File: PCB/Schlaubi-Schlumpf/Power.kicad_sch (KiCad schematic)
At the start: 33 parts, among them IC2 TP4056, IC3 TPS7A8801RTJR, IC7 LM2775QDSGRQ1, Q1 DMG2305

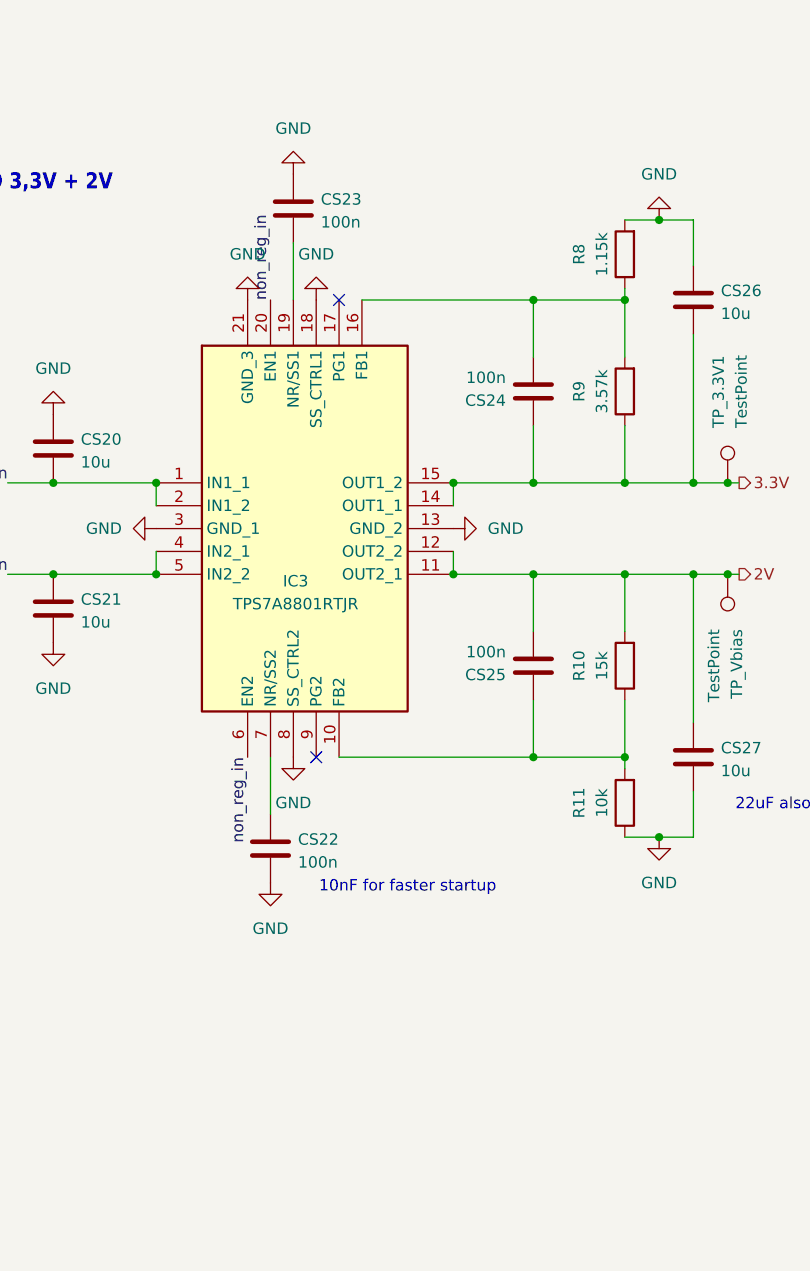
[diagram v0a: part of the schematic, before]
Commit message: added IMU
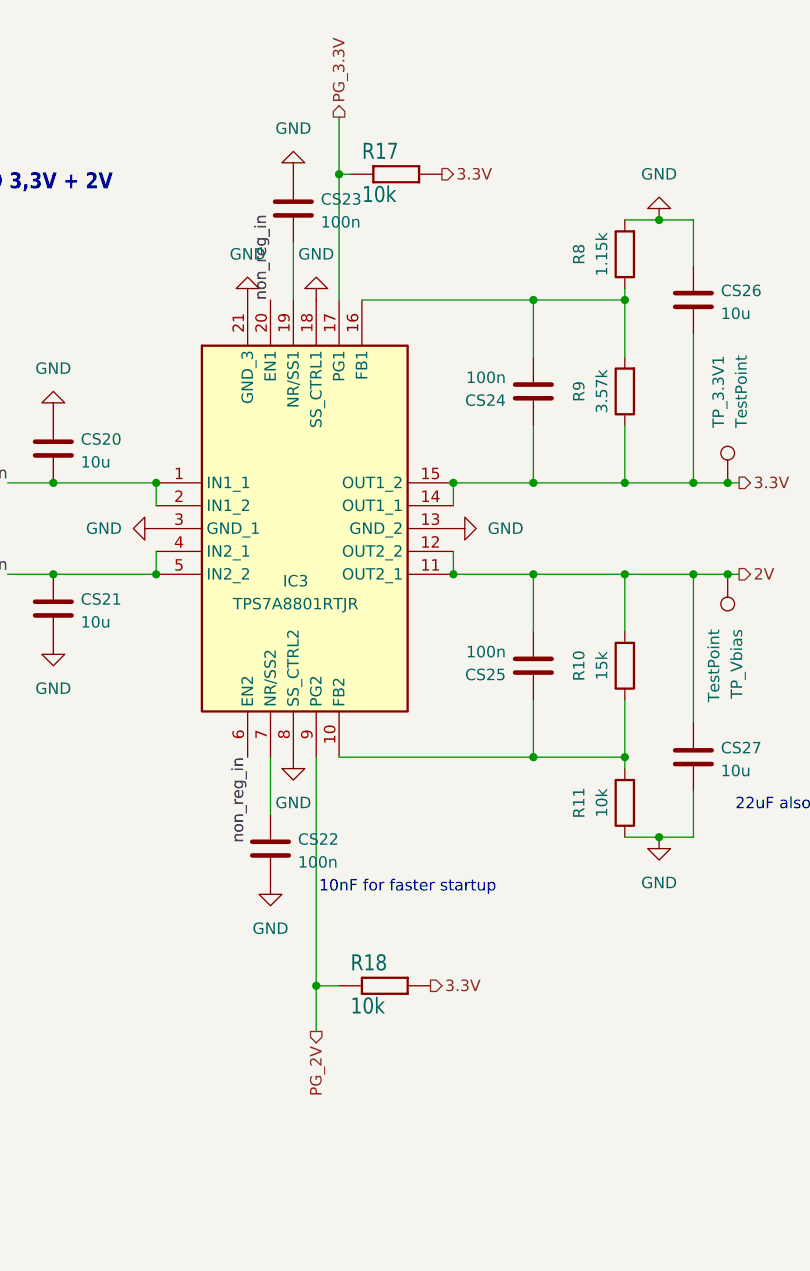
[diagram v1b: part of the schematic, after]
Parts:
- added R17, R18: 10k, Resistor_SMD:R_0603_1608Metric, symbol MiniLev-eagle-import:R-EU_R0805
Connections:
- net 3.3V: now also R17.2, R18.2
- net PG_3.3V: now reaches IC3.17 (PG1)
- net PG_3.3V: now also R17.1
- net PG_2V: now reaches IC3.9 (PG2)
- net PG_2V: now also R18.1
- no-connect marks 4 -> 2

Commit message: v1
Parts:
- removed R17, R18, R5: 10k, Resistor_SMD:R_0603_1608Metric, symbol MiniLev-eagle-import:R-EU_R0805
- added J4: Conn_01x02_Pin, Connector_JST:JST_PH_B2B-PH-K_1x02_P2.00mm_Vertical, symbol Connector:Conn_01x02_Pin
- added R17: 10k, Resistor_SMD:R_0603_1608Metric, symbol Device:R
- added TP_GND2: TestPoint, TestPoint:TestPoint_Pad_D1.0mm, symbol Connector:TestPoint
- C1: footprint Capacitor_SMD:C_0805_2012Metric -> Capacitor_SMD:C_0603_1608Metric
- CS22, CS23, CS24, CS25: value 100n -> 10n
- D2: value LED -> LED_R; footprint LED_SMD:LED_0805_2012Metric -> LED_SMD:LED_0603_1608Metric
- IC2: footprint MiniLev:SOP-8 -> TP4056:SOP127P600X175-9N
- IC3: footprint QFN50P400X400X80-21N-D -> TPS7A8801RTJR:QFN50P400X400X80-21N-D
- IC7: footprint SON50P200X200X80-9N -> LM2775QDSGRQ1:SON50P200X200X80-9N
- Q1: footprint MiniLev:SOT23-WIDE -> DMG2305UX:DMG2305UX
- TP_3.3V1: footprint TestPoint:TestPoint_THTPad_D1.0mm_Drill0.5mm -> TestPoint:TestPoint_Pad_D1.0mm
- TP_Vbias1: renamed from TP_Vbias; footprint TestPoint:TestPoint_THTPad_D1.0mm_Drill0.5mm -> TestPoint:TestPoint_Pad_D1.0mm
- renumbered C_Chargepump to CCHARGE1
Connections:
- net VBUS is gone; now on net Vbus: C8.1, D2.2 (A), IC2.4 (VCC), IC2.8 (CE)
- net Bat+: now also J4.2 (Pin_2)
- net GND: now also IC2.9 (EPAD), J4.1 (Pin_1), R17.1, TP_GND2.1
- net Vbus: now also R17.2
- net at C1.2, D1.1 (K), Q1.2 (S): now also S1.3; no longer S1.1
- net PG_2V: no longer names the net of IC3.9 (PG2)
- net PG_3.3V: no longer names the net of IC3.17 (PG1)
- no-connect marks 2 -> 4
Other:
- moved on the sheet: CS20, CS21, CS22, CS24, CS25, CS26, CS27, IC3, R10, R11, R8, R9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

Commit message: updates
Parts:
- CS22, CS23: value 10n -> 100n
- TP_3.3V1, TP_GND2, TP_Vbias1: footprint TestPoint:TestPoint_Pad_D1.0mm -> TestPoint:TestPoint_Pad_D1.5mm
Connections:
- net Bat+: now also J4.1 (Pin_1); no longer J4.2 (Pin_2)
- net GND: now also J4.2 (Pin_2); no longer J4.1 (Pin_1)
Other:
- moved on the sheet: J4, TP_GND2
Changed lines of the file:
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@@
 	(wire
 		(pts
+			(xy 105.41 93.98) (xy 105.41 99.06)
+		)
+		(stroke
+			(width 0)
+			(type default)
+		)
+	)
+	(wire
+		(pts
 			(xy 52.07 41.91) (xy 57.15 41.91)
 		)
@@
 	(wire
 		(pts
-			(xy 105.41 93.98) (xy 105.41 99.06)
-		)
-		(stroke
-			(width 0)
-			(type default)
-		)
-	)
-	(wire
-		(pts
 			(xy 44.45 99.06) (xy 46.99 99.06)
 		)
@@
 			)
 		)
-		(property "Footprint" "TestPoint:TestPoint_Pad_D1.0mm"
+		(property "Footprint" "TestPoint:TestPoint_Pad_D1.5mm"
 			(at 257.81 72.39 0)
 			(effects
@@
 	(symbol
 		(lib_id "Connector:TestPoint")
-		(at 278.13 64.77 0)
+		(at 233.68 152.4 0)
 		(unit 1)
 		(exclude_from_sim no)
@@
 		(dnp no)
 		(property "Reference" "TP_GND2"
-			(at 277.114 58.674 90)
+			(at 232.664 146.304 90)
 			(effects
 				(font
@@
 		)
 		(property "Value" "TestPoint"
-			(at 279.654 58.674 90)
+			(at 235.204 146.304 90)
 			(effects
 				(font
@@
 			)
 		)
-		(property "Footprint" "TestPoint:TestPoint_Pad_D1.0mm"
-			(at 283.21 64.77 0)
+		(property "Footprint" "TestPoint:TestPoint_Pad_D1.5mm"
+			(at 238.76 152.4 0)
 			(effects
 				(font
@@
 		)
 		(property "Datasheet" "~"
-			(at 283.21 64.77 0)
+			(at 238.76 152.4 0)
 			(effects
 				(font
@@
 		)
 		(property "Description" "test point"
-			(at 278.13 64.77 0)
+			(at 233.68 152.4 0)
 			(effects
 				(font
@@
 			)
 		)
-		(property "Footprint" "TestPoint:TestPoint_Pad_D1.0mm"
+		(property "Footprint" "TestPoint:TestPoint_Pad_D1.5mm"
 			(at 267.97 62.23 0)
 			(effects
@@
 			)
 		)
-		(property "Value" "10n"
+		(property "Value" "100n"
 			(at 215.138 104.394 0)
 			(effects
@@
 	(symbol
 		(lib_id "Connector:Conn_01x02_Pin")
-		(at 110.49 93.98 180)
+		(at 110.49 91.44 0)
+		(mirror y)
 		(unit 1)
 		(exclude_from_sim no)
@@
 		(dnp no)
 		(property "Reference" "J4"
-			(at 105.664 83.82 0)
+			(at 105.664 101.6 0)
 			(effects
 				(font
@@
 		)
 		(property "Value" "Conn_01x02_Pin"
-			(at 105.664 86.36 0)
+			(at 105.664 99.06 0)
 			(effects
 				(font
@@
 		)
 		(property "Footprint" "Connector_JST:JST_PH_B2B-PH-K_1x02_P2.00mm_Vertical"
-			(at 110.49 93.98 0)
+			(at 110.49 91.44 0)
 			(effects
 				(font
@@
 		)
 		(property "Datasheet" "~"
-			(at 110.49 93.98 0)
+			(at 110.49 91.44 0)
 			(effects
 				(font
@@
 		)
 		(property "Description" "Generic connector, single row, 01x02, script generated"
-			(at 110.49 93.98 0)
+			(at 110.49 91.44 0)
 			(effects
 				(font
@@
 			)
 		)
-		(property "Value" "10n"
+		(property "Value" "100n"
 			(at 217.678 33.274 0)
 			(effects
@@
 	(symbol
 		(lib_id "power:GND")
-		(at 278.13 64.77 0)
+		(at 233.68 152.4 0)
 		(unit 1)
 		(exclude_from_sim no)
@@
 		(fields_autoplaced yes)
 		(property "Reference" "#PWR062"
-			(at 278.13 71.12 0)
+			(at 233.68 158.75 0)
 			(effects
 				(font
@@
 		)
 		(property "Value" "GND"
-			(at 278.13 69.85 0)
+			(at 233.68 157.48 0)
 			(effects
 				(font
@@
 		)
 		(property "Footprint" ""
-			(at 278.13 64.77 0)
+			(at 233.68 152.4 0)
 			(effects
 				(font
@@
 		)
 		(property "Datasheet" ""
-			(at 278.13 64.77 0)
+			(at 233.68 152.4 0)
 			(effects
 				(font
@@
 		)
 		(property "Description" "Power symbol creates a global label with name \"GND\" , ground"
-			(at 278.13 64.77 0)
+			(at 233.68 152.4 0)
 			(effects
 				(font

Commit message: update Opamp
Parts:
- removed CS20, CS21, CS26, CS27: 10u, Capacitor_SMD:C_0603_1608Metric, symbol Device:C
- removed CS22, CS23: 100n, Capacitor_SMD:C_0603_1608Metric, symbol Device:C
- removed CS24, CS25: 10n, Capacitor_SMD:C_0603_1608Metric, symbol Device:C
- removed IC3: TPS7A8801RTJR, TPS7A8801RTJR:QFN50P400X400X80-21N-D, symbol TPS7A8801RTJR:TPS7A8801RTJR
- removed R10: 15k, Resistor_SMD:R_0603_1608Metric, symbol Device:R
- removed R11: 10k, Resistor_SMD:R_0603_1608Metric, symbol Device:R
- removed R8: 1.15k, Resistor_SMD:R_0603_1608Metric, symbol Device:R
- removed R9: 3.57k, Resistor_SMD:R_0603_1608Metric, symbol Device:R
- removed TP_3.3V1, TP_Vbias1: TestPoint, TestPoint:TestPoint_Pad_D1.5mm, symbol Connector:TestPoint
- added CS31, CS34: 10u, Capacitor_SMD:C_0603_1608Metric, symbol Device:C
- added CS32: 100n, Capacitor_SMD:C_0603_1608Metric, symbol Device:C
- added CS33: 10n, Capacitor_SMD:C_0603_1608Metric, symbol Device:C
- added IC5: TPS7A9101DSKR, TPS7A9101DSKR:SON50P250X250X80-11N-D, symbol TPS7A9101DSKR:TPS7A9101DSKR
- added R32: 1.15k, Resistor_SMD:R_0603_1608Metric, symbol Device:R
- added R33: 3.57k, Resistor_SMD:R_0603_1608Metric, symbol Device:R
- added TP_3.3V2: TestPoint, TestPoint:TestPoint_Pad_D1.5mm, symbol Connector:TestPoint
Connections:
- net 3.3V: now also CS33.2, CS34.1, IC5.1 (OUT_1), IC5.2 (OUT_2), R33.1, TP_3.3V2.1
- net GND: now also CS31.2, CS32.2, CS34.2, IC5.11 (GND_2), IC5.4 (GND_1), IC5.6 (SS_CTRL), R32.2
- net non_reg_in: now also CS31.1, IC5.10 (IN_2), IC5.7 (EN), IC5.9 (IN_1)
- new net: CS33.1, IC5.3 (FB), R32.1, R33.2
- new net: CS32.1, IC5.8 (NR/SS)
- no-connect marks 4 -> 3
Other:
- note added: "LDO"
- note removed: "10nF for faster startup"
- note removed: "22uF also possible"
- note removed: "LDO 3,3V + 2V"

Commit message: newest order 17.09
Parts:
- TP_3.3V2, TP_GND2: footprint TestPoint:TestPoint_Pad_D1.5mm -> TestPoint:TestPoint_Pad_D1.0mm
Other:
- note added: "Integrated Polarity Protection"
- note added: "R1"
- note added: "R2"
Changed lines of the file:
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@@
 (kicad_sch
-	(version 20231120)
+	(version 20250114)
 	(generator "eeschema")
-	(generator_version "8.0")
+	(generator_version "9.0")
 	(paper "A4")
+	(text "R1 = (Vout/0,8 - 1) * R2"
+		(exclude_from_sim no)
+		(at 265.176 82.55 0)
+		(effects
+			(font
+				(size 1.27 1.27)
+			)
+		)
+	)
+	(text "R2\n"
+		(exclude_from_sim no)
+		(at 231.648 73.152 0)
+		(effects
+			(font
+				(size 1.27 1.27)
+			)
+		)
+	)
+	(text "PFM disabled for \nnoise reduction"
+		(exclude_from_sim no)
+		(at 130.048 158.242 0)
+		(effects
+			(font
+				(size 1.27 1.27)
+			)
+		)
+	)
+	(text "Input Switch"
+		(exclude_from_sim no)
+		(at 27.178 24.384 0)
+		(effects
+			(font
+				(size 1.778 1.5113)
+				(thickness 0.3023)
+				(bold yes)
+			)
+			(justify left bottom)
+		)
+	)
+	(text "Battery Charger"
+		(exclude_from_sim no)
+		(at 25.4 74.295 0)
+		(effects
+			(font
+				(size 1.778 1.5113)
+				(thickness 0.3023)
+				(bold yes)
+			)
+			(justify left bottom)
+		)
+	)
+	(text "LDO"
+		(exclude_from_sim no)
+		(at 156.718 20.574 0)
+		(effects
+			(font
+				(size 1.778 1.5113)
+				(thickness 0.3023)
+				(bold yes)
+			)
+			(justify left bottom)
+		)
+	)
+	(text "R1"
+		(exclude_from_sim no)
+		(at 231.648 57.404 0)
+		(effects
+			(font
+				(size 1.27 1.27)
+			)
+		)
+	)
+	(text "5V Charge Pump"
+		(exclude_from_sim no)
+		(at 25.4 137.16 0)
+		(effects
+			(font
+				(size 1.778 1.5113)
+				(thickness 0.3023)
+				(bold yes)
+			)
+			(justify left bottom)
+		)
+	)
+	(text "Integrated Polarity Protection"
+		(exclude_from_sim no)
+		(at 87.63 87.63 0)
+		(effects
+			(font
+				(size 1.27 1.27)
+			)
+		)
+	)
 	(junction
 		(at 63.5 154.94)
@@
 		)
 	)
-	(text "R1 = (Vout/0,8 - 1) * R2"
-		(exclude_from_sim no)
-		(at 281.686 80.01 0)
-		(effects
-			(font
-				(size 1.27 1.27)
-			)
-		)
-	)
-	(text "PFM disabled for \nnoise reduction"
-		(exclude_from_sim no)
-		(at 130.048 158.242 0)
-		(effects
-			(font
-				(size 1.27 1.27)
-			)
-		)
-	)
-	(text "Input Switch"
-		(exclude_from_sim no)
-		(at 27.178 24.384 0)
-		(effects
-			(font
-				(size 1.778 1.5113)
-				(thickness 0.3023)
-				(bold yes)
-			)
-			(justify left bottom)
-		)
-	)
-	(text "Battery Charger"
-		(exclude_from_sim no)
-		(at 25.4 74.295 0)
-		(effects
-			(font
-				(size 1.778 1.5113)
-				(thickness 0.3023)
-				(bold yes)
-			)
-			(justify left bottom)
-		)
-	)
-	(text "LDO"
-		(exclude_from_sim no)
-		(at 156.718 20.574 0)
-		(effects
-			(font
-				(size 1.778 1.5113)
-				(thickness 0.3023)
-				(bold yes)
-			)
-			(justify left bottom)
-		)
-	)
-	(text "5V Charge Pump"
-		(exclude_from_sim no)
-		(at 25.4 137.16 0)
-		(effects
-			(font
-				(size 1.778 1.5113)
-				(thickness 0.3023)
-				(bold yes)
-			)
-			(justify left bottom)
-		)
-	)
 	(label "non_reg_in"
 		(at 96.52 50.8 180)
-		(fields_autoplaced yes)
 		(effects
 			(font
@@
 	(label "non_reg_in"
 		(at 92.71 39.37 0)
-		(fields_autoplaced yes)
 		(effects
 			(font
@@
 	(label "non_reg_in"
 		(at 158.75 46.99 180)
-		(fields_autoplaced yes)
 		(effects
 			(font
@@
 	(label "non_reg_in"
 		(at 36.83 154.94 180)
-		(fields_autoplaced yes)
 		(effects
 			(font
@@
 	(label "Bat+"
 		(at 95.25 91.44 0)
-		(fields_autoplaced yes)
 		(effects
 			(font
@@
 	(label "Bat+"
 		(at 57.15 25.4 0)
-		(fields_autoplaced yes)
 		(effects
 			(font
@@
 		(shape output)
 		(at 267.97 46.99 0)
-		(fields_autoplaced yes)
 		(effects
 			(font
@@
 		(shape input)
 		(at 35.56 35.56 180)
-		(fields_autoplaced yes)
 		(effects
 			(font
@@
 		(shape output)
 		(at 100.33 50.8 0)
-		(fields_autoplaced yes)
 		(effects
 			(font
@@
 		(shape input)
 		(at 31.75 91.44 180)
-		(fields_autoplaced yes)
 		(effects
 			(font
@@
 		(shape output)
 		(at 36.83 157.48 180)
-		(fields_autoplaced yes)
 		(effects
 			(font
@@
 			)
 		)
-		(property "Footprint" "TestPoint:TestPoint_Pad_D1.5mm"
+		(property "Footprint" "TestPoint:TestPoint_Pad_D1.0mm"
 			(at 238.76 152.4 0)
 			(effects
@@
 			)
 		)
-		(property "Footprint" "TestPoint:TestPoint_Pad_D1.5mm"
+		(property "Footprint" "TestPoint:TestPoint_Pad_D1.0mm"
 			(at 267.97 46.99 0)
 			(effects
